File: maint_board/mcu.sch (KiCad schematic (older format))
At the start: 22 parts, among them J3 TC2030-IDC_FB, SW1 SW_PUSH, U1 ATMEGA32U4, X1 XTAL_GND

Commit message: added libs and worked on layout
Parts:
- SW1: symbol keyboard_parts:SW_PUSH -> maint_board-rescue:SW_PUSH-keyboard_parts
- U1: symbol keyboard_parts:ATMEGA32U4 -> maint_board-rescue:ATMEGA32U4-keyboard_parts
- X1: symbol keyboard_parts:XTAL_GND -> maint_board-rescue:XTAL_GND-keyboard_parts
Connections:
- net labels removed: Col7, Row5
- wire segments 127 -> 125
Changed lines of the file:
@@
 	7200 3350 7000 3350
-Wire Wire Line
-	7000 3450 7200 3450
 Wire Wire Line
 	7900 3750 8000 3750
@@
 Text HLabel 7200 3350 2    50   Input ~ 0
 Row4
-Text HLabel 7200 3450 2    50   Input ~ 0
-Row5
 Text HLabel 7200 4450 2    50   Input ~ 0
 Col1
@@
 Text HLabel 7200 3950 2    50   Input ~ 0
 Col6
-Text HLabel 7200 3550 2    50   Input ~ 0
-Col7
 Text HLabel 1250 2950 0    50   Input ~ 0
 usb_D-
@@
 	3850 4550 4850 4550
 $Comp
-L keyboard_parts:ATMEGA32U4 U1
+L maint_board-rescue:ATMEGA32U4-keyboard_parts U1
 U 1 1 601CBA26
 P 5900 3800
+AR Path="/601CBA26" Ref="U1"  Part="1"
+AR Path="/6012B71A/601CBA26" Ref="U1"  Part="1"
 F 0 "U1" H 5925 5137 60  0000 C CNN
 F 1 "ATMEGA32U4" H 5925 5031 60  0000 C CNN
@@
 $EndComp
 $Comp
-L keyboard_parts:XTAL_GND X1
+L maint_board-rescue:XTAL_GND-keyboard_parts X1
 U 1 1 6022D139
 P 1650 4350
@@
 $EndComp
 $Comp
-L keyboard_parts:SW_PUSH SW1
+L maint_board-rescue:SW_PUSH-keyboard_parts SW1
 U 1 1 6023273D
 P 2550 3950
@@
 	7200 4450 7000 4450
 Wire Wire Line
-	7200 3550 7000 3550
-Wire Wire Line
 	7200 4150 7000 4150

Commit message: Finiched!
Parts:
- added D7: LED, Diode_SMD:D_0603_1608Metric, symbol Device:LED
- added Q1: Q_NMOS_GSD, Package_TO_SOT_SMD:SOT-23, symbol Device:Q_NMOS_GSD
- added R10: 10k, Resistor_SMD:R_0603_1608Metric, symbol Device:R
- added R9: 500, Resistor_SMD:R_0603_1608Metric, symbol Device:R
- J3: footprint my_connectors:TC2030-IDC-FP -> Connector:Tag-Connect_TC2030-IDC-NL_2x03_P1.27mm_Vertical
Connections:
- net GND: now also Q1.2 (S), R10.2
- net VCC: now also R9.1
- net at U1.37 (PF6): now also Q1.1 (G), R10.1
- new net: D7.1 (K), Q1.3 (D)
- new net: D7.2 (A), R9.2
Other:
- moved on the sheet: C3, C4, C5, C6, C7

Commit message: commit before reinstall computer
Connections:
- net rst_prog: now also R1.2, SW1.2, U1.13 (~RESET); no longer U1.12 (PB7/~RTS)
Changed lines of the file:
@@
 	1950 4250 4850 4250
 Wire Wire Line
-	4850 3950 3000 3950
+	4850 3950 3800 3950
 Wire Wire Line
 	3550 5200 4050 5200
@@
 Text GLabel 4600 3550 0    50   Input ~ 0
 sck_prog
-Text GLabel 4600 3850 0    50   Input ~ 0
+Text GLabel 3800 3800 1    50   Input ~ 0
 rst_prog
-Wire Wire Line
-	4850 3850 4600 3850
 Wire Wire Line
 	4600 3750 4850 3750
@@
 	1    0    0    -1
 $EndComp
+Wire Wire Line
+	3800 3800 3800 3950
+Connection ~ 3800 3950
+Wire Wire Line
+	3800 3950 3000 3950
 $EndSCHEMATC

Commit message: updated submodule
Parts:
- SW1: symbol maint_board-rescue:SW_PUSH-keyboard_parts -> maint_board-rescue:SW_PUSH-keyboard_parts-maint_board-rescue
- U1: symbol maint_board-rescue:ATMEGA32U4-keyboard_parts -> maint_board-rescue:ATMEGA32U4-keyboard_parts-maint_board-rescue
- X1: symbol maint_board-rescue:XTAL_GND-keyboard_parts -> maint_board-rescue:XTAL_GND-keyboard_parts-maint_board-rescue
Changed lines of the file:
@@
 	3850 4550 4850 4550
 $Comp
-L maint_board-rescue:ATMEGA32U4-keyboard_parts U1
+L maint_board-rescue:ATMEGA32U4-keyboard_parts-maint_board-rescue U1
 U 1 1 601CBA26
 P 5900 3800
@@
 $EndComp
 $Comp
-L maint_board-rescue:XTAL_GND-keyboard_parts X1
+L maint_board-rescue:XTAL_GND-keyboard_parts-maint_board-rescue X1
 U 1 1 6022D139
 P 1650 4350
@@
 $EndComp
 $Comp
-L maint_board-rescue:SW_PUSH-keyboard_parts SW1
+L maint_board-rescue:SW_PUSH-keyboard_parts-maint_board-rescue SW1
 U 1 1 6023273D
 P 2550 3950

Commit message: this is before I switch to usb C
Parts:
- added J4: Conn_01x04, Connector_PinHeader_1.00mm:PinHeader_1x04_P1.00mm_Vertical, symbol Connector_Generic:Conn_01x04
- added JP1, JP2, JP3: SolderJumper_2_Open, Jumper:SolderJumper-2_P1.3mm_Open_RoundedPad1.0x1.5mm, symbol Jumper:SolderJumper_2_Open
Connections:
- net GND: now also J4.1 (Pin_1)
- net Row1: now also U1.36 (PF7); no longer U1.41 (PF0)
- net SCL: now also JP1.2 (B); no longer U1.18 (PD0/INT0)
- net SDA: now also JP2.1 (A), JP3.1 (A); no longer U1.19 (PD1/INT1)
- net VCC: now also J4.4 (Pin_4)
- net serial: now reaches U1.20 (PD2/RXD1)
- net serial: now also JP3.2 (B)
- net Vbus: now reaches U1.7 (VBus)
- new net i2c_scl: J4.3 (Pin_3), JP1.1 (A), U1.18 (PD0/INT0)
- new net i2c_sda: J4.2 (Pin_2), JP2.2 (B), U1.19 (PD1/INT1)
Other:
- moved on the sheet: C8, R4, R5

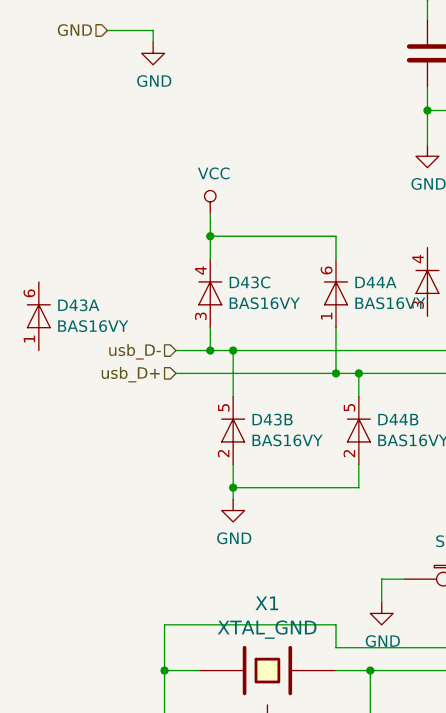
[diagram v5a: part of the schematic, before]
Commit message: added filter on usb shield
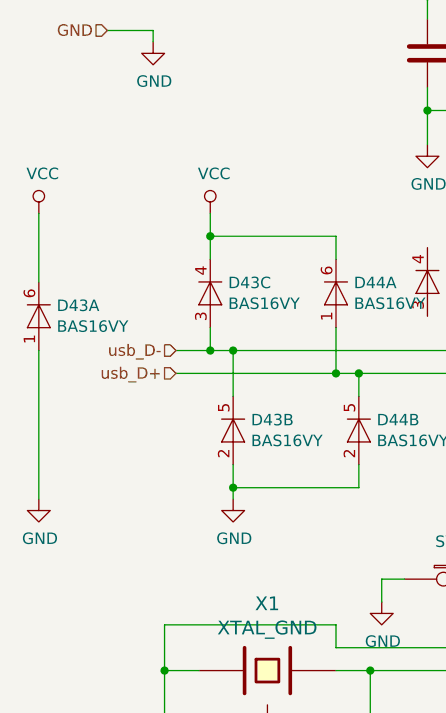
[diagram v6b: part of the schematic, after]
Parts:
- R10, R9: footprint Resistor_SMD:R_0603_1608Metric -> Resistor_SMD:R_0603_1608Metric_Pad1.05x0.95mm_HandSolder
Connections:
- net GND: now also D43.1 (A)
- net VCC: now also D43.6 (K)
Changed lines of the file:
@@
 F 0 "R9" H 9070 2646 50  0000 L CNN
 F 1 "500" H 9070 2555 50  0000 L CNN
-F 2 "Resistor_SMD:R_0603_1608Metric" V 8930 2600 50  0001 C CNN
+F 2 "Resistor_SMD:R_0603_1608Metric_Pad1.05x0.95mm_HandSolder" V 8930 2600 50  0001 C CNN
 F 3 "~" H 9000 2600 50  0001 C CNN
 	1    9000 2600
@@
 F 0 "R10" H 8670 3746 50  0000 L CNN
 F 1 "10k" H 8670 3655 50  0000 L CNN
-F 2 "Resistor_SMD:R_0603_1608Metric" V 8530 3700 50  0001 C CNN
+F 2 "Resistor_SMD:R_0603_1608Metric_Pad1.05x0.95mm_HandSolder" V 8530 3700 50  0001 C CNN
 F 3 "~" H 8600 3700 50  0001 C CNN
 	1    8600 3700
@@
 Wire Wire Line
 	2200 6000 2200 6100
+$Comp
+L power:VCC #PWR?
+U 1 1 61A03129
+P 650 2350
+AR Path="/61A03129" Ref="#PWR?"  Part="1"
+AR Path="/6012B71A/61A03129" Ref="#PWR0101"  Part="1"
+F 0 "#PWR0101" H 650 2200 50  0001 C CNN
+F 1 "VCC" H 667 2523 50  0000 C CNN
+F 2 "" H 650 2350 50  0001 C CNN
+F 3 "" H 650 2350 50  0001 C CNN
+	1    650  2350
+	1    0    0    -1
+$EndComp
+$Comp
+L power:GND #PWR?
+U 1 1 61A03653
+P 650 3600
+AR Path="/61A03653" Ref="#PWR?"  Part="1"
+AR Path="/6012B71A/61A03653" Ref="#PWR0102"  Part="1"
+F 0 "#PWR0102" H 650 3350 50  0001 C CNN
+F 1 "GND" H 655 3427 50  0000 C CNN
+F 2 "" H 650 3600 50  0001 C CNN
+F 3 "" H 650 3600 50  0001 C CNN
+	1    650  3600
+	1    0    0    -1
+$EndComp
+Wire Wire Line
+	650  3600 650  2950
+Wire Wire Line
+	650  2650 650  2350
 $EndSCHEMATC

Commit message: added som libes
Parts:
- added R14: 330, Resistor_SMD:R_0603_1608Metric_Pad1.05x0.95mm_HandSolder, symbol Device:R
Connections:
- net rst_prog: now also R14.1; no longer R1.2, SW1.2
- new net: R1.2, R14.2, SW1.2
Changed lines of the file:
@@
 Connection ~ 3800 3950
 Wire Wire Line
-	3800 3950 3000 3950
+	3800 3950 3550 3950
 Wire Wire Line
 	4600 3350 4850 3350
@@
 Wire Wire Line
 	650  2650 650  2350
+$Comp
+L Device:R R14
+U 1 1 61A206B7
+P 3400 3950
+F 0 "R14" V 3193 3950 50  0000 C CNN
+F 1 "330" V 3284 3950 50  0000 C CNN
+F 2 "Resistor_SMD:R_0603_1608Metric_Pad1.05x0.95mm_HandSolder" V 3330 3950 50  0001 C CNN
+F 3 "~" H 3400 3950 50  0001 C CNN
+	1    3400 3950
+	0    1    1    0
+$EndComp
+Wire Wire Line
+	3250 3950 3000 3950
 $EndSCHEMATC
